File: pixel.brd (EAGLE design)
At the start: 160 x 100 mm, 13 parts, among them IC1 STM32F030K6TX-LQFP32(7X7), Y1 8 MHz

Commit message: blah
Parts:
- removed Y1: 8 MHz, crystals:CRYSTAL_SMD_3.2X2.5MM
- added C11: 0.1uF, rc:C0603
- added C12: 100 nF, rc:C0603
- added C13: 1nF, rc:C1206
- added CON1, CON2: DS1066-07M-SIDE, pixel_masterlib:DS1066-08M_SIDE
- added D1: SMF05C, pixel_masterlib:SC70_6L
- added D2: SMAJ12A, masterlib:SMA
- added IC2: ESDA6V1L, pixel_masterlib:SOT23
- added IC3: ST3485SOIC8, pixel_masterlib:SOIC8
- added IC4, IC5: MC74VHC1GT125, pixel_masterlib:SOT23-5
- added L1: 47UH, power_inductors:SDR0604
- added Q1: FDC6420C, pixel_masterlib:SOT23-6
- added R11, R12, R4, R5: 22R, rc:R0805
- added R2, R3: 560R, rc:R0603
- added R6: 10K, rc:R0805
- added R9: 60R, rc:R0603
- added RN1, RN2: 510R, pixel_masterlib:CAT16-J4
- added SJ1, SJ2: (no value), eth_conv_master_lib:RES_0
- added Z1: 16MHz, watchdog_master_library:OSCILLATOR-3.2X2.5
- C1: value 4.7 uF -> 100 nF
- R1: value (none) -> 60R
- moved C1 51.1 mm to (-18.0, -62.0)
- moved IC1 29.4 mm to (-6.00, -33.0)
- moved C2 28.3 mm to (-6.00, -46.0)
- moved C4 24.8 mm to (18.0, -46.0)
- moved C3 23.6 mm to (-2.00, -46.0)
- moved C5 18.2 mm to (12.0, -46.0)
- moved R1 15.9 mm to (-11.0, -50.0)
- moved C7 11.7 mm to (2.00, -46.0)
- moved C8 8.62 mm to (6.00, -46.0)
- moved C6 7.65 mm to (9.00, -46.0)
- moved C10 4.84 mm to (4.00, -50.0)
- moved C9 1.74 mm to (1.00, -50.0)
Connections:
- net LED1_FB renamed RE/DE
- new net A: D2.A, IC2.2, IC3.6, R1.2, R11.1, R11.2, R3.2
- new net B: D2.C, IC2.3, IC3.7, R12.1, R12.2, R2.1, SJ2.1
- new net CLOCK_BUFFERED: IC4.4, RN2.2
- new net DATA_IN: D1.4, RN1.1
- new net DATA_OUT: RN2.1
- new net DE: IC3.2, IC3.3
- new net LATCH_BUFFERED: IC5.4, RN2.3
- new net N$10: R9.1, SJ2.2
- new net N$11: C13.P$1, SJ1.2
- new net N$12: CON2.6, RN2.6
- new net N$13: Q1.1, R4.2
- new net N$14: R4.1
- new net N$15: Q1.6, R5.1
- new net N$16: Q1.2
- new net N$4: CON1.5, RN1.7
- new net N$5: CON1.6, RN1.6
- new net N$6: CON2.4, RN2.8
- new net N$7: Q1.3, R5.2, R6.2
- new net N$8: R1.1, R9.2, SJ1.1
- new net N$9: CON2.5, RN2.7
- new net RS485_A: CON1.2, CON2.2
- new net RS485_B: CON1.3, CON2.3
- new net VDD_12V: Q1.4, R6.1
- new net VDD_24V: CON1.1, CON2.1
- net CLOCK: now also D1.5, IC4.2, RN1.2
- net GND: now also C10.2, C11.1, C12.1, C13.P$2, CON1.7, CON2.7, D1.2, IC2.1, IC3.5, IC4.3, IC5.3, Q1.5, R3.1, Z1.2, Z1.4; no longer C10.1, Y1.2, Y1.4
- net LATCH: now also D1.6, IC5.2, RN1.3
- net N$1: now also Z1.1; no longer Y1.3
- net N$2: now also CON1.4, RN1.8; no longer IC1.3, R1.1
- net N$3: now also C10.1, IC1.3, Z1.3; no longer C10.2, R1.2, Y1.1
- net RX: now also IC3.1
- net TX: now also IC3.4
- net VDD_3V3: now also C11.2, C12.2, IC3.8, IC4.5, IC5.5, R2.2
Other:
- board outline removed

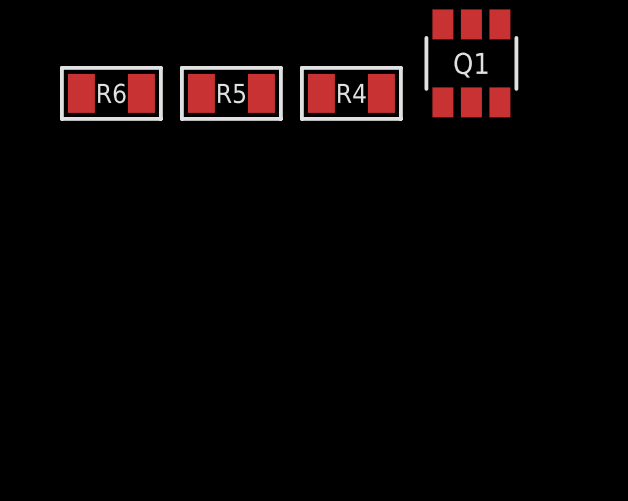
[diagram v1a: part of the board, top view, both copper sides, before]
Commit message: Preliminary LED driver
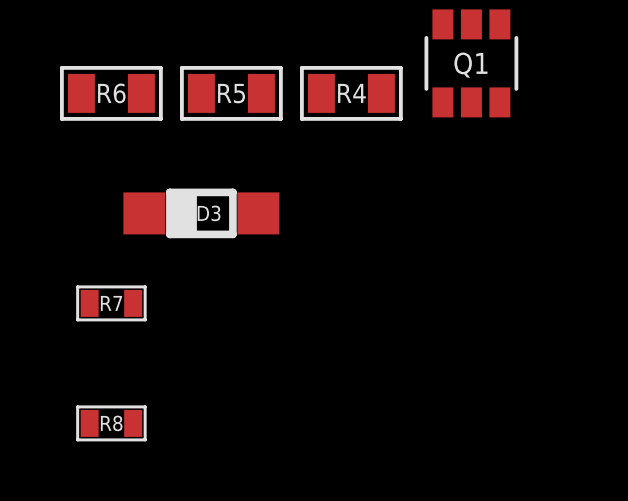
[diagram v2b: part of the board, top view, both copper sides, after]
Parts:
- added D3: (no value), diodes:SOD123
- added R7, R8: (no value), rc:R0603
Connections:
- removed net N$14: R4.1
- removed net N$16: Q1.2
- new net LED1_A: L1.2
- new net LED1_FB\: R7.1
- new net LED_COMMON_C: R7.2, R8.2
- new net N$17: D3.C, L1.1, Q1.2
- net GND: now also D3.A, R8.1
- net LED1_PWM: now also R4.1
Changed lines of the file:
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@@
 <attribute name="PACKAGE" value="0805" x="-46" y="-65" size="1.778" layer="27" display="off"/>
+</element>
+<element name="D3" library="diodes" package="SOD123" value="" x="-43" y="-69">
+<attribute name="PACKAGE" value="SOD123" x="-43" y="-69" size="1.778" layer="27" display="off"/>
+</element>
+<element name="R7" library="rc" package="R0603" value="" x="-46" y="-72">
+<attribute name="PACKAGE" value="0603" x="-46" y="-72" size="1.778" layer="27" display="off"/>
+</element>
+<element name="R8" library="rc" package="R0603" value="" x="-46" y="-76">
+<attribute name="PACKAGE" value="0603" x="-46" y="-76" size="1.778" layer="27" display="off"/>
 </element>
 </elements>
@@
 <contactref element="C12" pad="1"/>
 <contactref element="Q1" pad="5"/>
+<contactref element="D3" pad="A"/>
+<contactref element="R8" pad="1"/>
+<wire x1="-41.1" y1="-69" x2="-46.725" y2="-76" width="0" layer="19" extent="1-1"/>
+<wire x1="-34" y1="-62.7" x2="-41.1" y2="-69" width="0" layer="19" extent="1-1"/>
 <wire x1="-18.725" y1="-62" x2="-34" y2="-62.7" width="0" layer="19" extent="1-1"/>
 <wire x1="-18.725" y1="-66" x2="-18.725" y2="-62" width="0" layer="19" extent="1-1"/>
@@
 <signal name="LED1_PWM">
 <contactref element="IC1" pad="18"/>
+<contactref element="R4" pad="1"/>
+<wire x1="-1.75" y1="-35" x2="-39" y2="-65" width="0" layer="19" extent="1-1"/>
 </signal>
 <signal name="LED2_PWM">
@@
 <wire x1="-34.95" y1="-65.3" x2="-37" y2="-65" width="0" layer="19" extent="1-1"/>
 </signal>
-<signal name="N$14">
-<contactref element="R4" pad="1"/>
-</signal>
 <signal name="VDD_12V">
 <contactref element="Q1" pad="4"/>
 <contactref element="R6" pad="1"/>
 <wire x1="-33.05" y1="-62.7" x2="-47" y2="-65" width="0" layer="19" extent="1-1"/>
-</signal>
-<signal name="N$16">
-<contactref element="Q1" pad="2"/>
 </signal>
 <signal name="N$7">
@@
 <wire x1="-34.95" y1="-62.7" x2="-43" y2="-65" width="0" layer="19" extent="1-1"/>
 </signal>
+<signal name="N$17">
+<contactref element="D3" pad="C"/>
+<contactref element="Q1" pad="2"/>
+<contactref element="L1" pad="1"/>
+<wire x1="-34" y1="-65.3" x2="-44.9" y2="-69" width="0" layer="19" extent="1-1"/>
+<wire x1="-29.95" y1="-57" x2="-34" y2="-65.3" width="0" layer="19" extent="1-1"/>
+</signal>
+<signal name="LED1_FB\">
+<contactref element="R7" pad="1"/>
+</signal>
+<signal name="LED1_A">
+<contactref element="L1" pad="2"/>
+</signal>
+<signal name="LED_COMMON_C">
+<contactref element="R8" pad="2"/>
+<contactref element="R7" pad="2"/>
+<wire x1="-45.275" y1="-72" x2="-45.275" y2="-76" width="0" layer="19" extent="1-1"/>
+</signal>
 </signals>

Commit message: minor changes
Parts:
- removed D3: (no value), diodes:SOD123
- removed R8: (no value), rc:R0603
- added C14: 10uF 6.3V, rc:C1206
- added D4: CRS08-SOD123, eth_conv_master_lib:SOD123
- added NRF24L01: NRF24L01, ali_modules:NRF24L01
- R7: value (none) -> 2R; device rc:R0603 -> rc:R1206
- moved R7 4.47 mm to (-50.0, -74.0)
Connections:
- removed net LED1_A: L1.2
- removed net LED1_FB\: R7.1
- removed net LED_COMMON_C: R7.2, R8.2
- new net MISO: IC1.27, NRF24L01.7
- new net MOSI: IC1.28, NRF24L01.6
- new net NRF_CE: NRF24L01.3
- new net NRF_CSN: NRF24L01.4
- new net NRF_IRQ: NRF24L01.8
- new net SCK: IC1.26, NRF24L01.5
- net GND: now also C14.P$2, D4.A, NRF24L01.1, R7.P$1; no longer D3.A, R8.1
- net N$17: now also D4.C; no longer D3.C
- net VDD_3V3: now also C14.P$1, NRF24L01.2
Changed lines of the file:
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@@
 <attribute name="PACKAGE" value="0805" x="-46" y="-65" size="1.778" layer="27" display="off"/>
 </element>
-<element name="D3" library="diodes" package="SOD123" value="" x="-43" y="-69">
-<attribute name="PACKAGE" value="SOD123" x="-43" y="-69" size="1.778" layer="27" display="off"/>
+<element name="R7" library="rc" package="R1206" value="2R" x="-50" y="-74">
+<attribute name="PACKAGE" value="1206" x="-50" y="-74" size="1.778" layer="27" display="off"/>
 </element>
-<element name="R7" library="rc" package="R0603" value="" x="-46" y="-72">
-<attribute name="PACKAGE" value="0603" x="-46" y="-72" size="1.778" layer="27" display="off"/>
+<element name="D4" library="eth_conv_master_lib" package="SOD123" value="CRS08-SOD123" x="-47" y="-78">
+<attribute name="MANF#" value="CRS08(TE85L,Q,M)" x="-47" y="-78" size="1.778" layer="27" display="off"/>
+<attribute name="MANF" value="Toshiba Semiconductor and Storage" x="-47" y="-78" size="1.778" layer="27" display="off"/>
+<attribute name="DIGIKEY#" value="CRS08QMCT-ND" x="-47" y="-78" size="1.778" layer="27" display="off"/>
 </element>
-<element name="R8" library="rc" package="R0603" value="" x="-46" y="-76">
-<attribute name="PACKAGE" value="0603" x="-46" y="-76" size="1.778" layer="27" display="off"/>
+<element name="NRF24L01" library="ali_modules" package="NRF24L01" value="NRF24L01" x="-30" y="-95"/>
+<element name="C14" library="rc" package="C1206" value="10uF 6.3V" x="-50" y="-108">
+<attribute name="PACKAGE" value="1206" x="-55" y="-102" size="1.778" layer="27" display="off"/>
 </element>
 </elements>
@@
 <contactref element="IC5" pad="5"/>
 <contactref element="C12" pad="2"/>
+<contactref element="NRF24L01" pad="2"/>
+<contactref element="C14" pad="P$1"/>
+<wire x1="-40.16" y1="-88.65" x2="-51.55" y2="-108" width="0" layer="19" extent="1-1"/>
+<wire x1="-17.275" y1="-66" x2="-40.16" y2="-88.65" width="0" layer="19" extent="1-1"/>
 <wire x1="-17.275" y1="-62" x2="-17.275" y2="-66" width="0" layer="19" extent="1-1"/>
 <wire x1="-15.95" y1="-54.7" x2="-17.275" y2="-62" width="0" layer="19" extent="1-1"/>
@@
 </signal>
 <signal name="GND">
-<contactref element="C2" pad="1"/>
 <contactref element="C3" pad="1"/>
 <contactref element="C4" pad="1"/>
@@
 <contactref element="C12" pad="1"/>
 <contactref element="Q1" pad="5"/>
-<contactref element="D3" pad="A"/>
-<contactref element="R8" pad="1"/>
-<wire x1="-41.1" y1="-69" x2="-46.725" y2="-76" width="0" layer="19" extent="1-1"/>
-<wire x1="-34" y1="-62.7" x2="-41.1" y2="-69" width="0" layer="19" extent="1-1"/>
+<contactref element="R7" pad="P$1"/>
+<contactref element="D4" pad="A"/>
+<contactref element="NRF24L01" pad="1"/>
+<contactref element="C14" pad="P$2"/>
+<contactref element="C2" pad="1"/>
+<wire x1="-42.7" y1="-88.65" x2="-48.45" y2="-108" width="0" layer="19" extent="1-1"/>
+<wire x1="-45.3" y1="-78" x2="-42.7" y2="-88.65" width="0" layer="19" extent="1-1"/>
+<wire x1="-51.55" y1="-74" x2="-45.3" y2="-78" width="0" layer="19" extent="1-1"/>
+<wire x1="-34" y1="-62.7" x2="-45.3" y2="-78" width="0" layer="19" extent="1-1"/>
 <wire x1="-18.725" y1="-62" x2="-34" y2="-62.7" width="0" layer="19" extent="1-1"/>
 <wire x1="-18.725" y1="-66" x2="-18.725" y2="-62" width="0" layer="19" extent="1-1"/>
@@
 </signal>
 <signal name="N$17">
-<contactref element="D3" pad="C"/>
 <contactref element="Q1" pad="2"/>
 <contactref element="L1" pad="1"/>
-<wire x1="-34" y1="-65.3" x2="-44.9" y2="-69" width="0" layer="19" extent="1-1"/>
+<contactref element="D4" pad="C"/>
+<wire x1="-34" y1="-65.3" x2="-48.7" y2="-78" width="0" layer="19" extent="1-1"/>
 <wire x1="-29.95" y1="-57" x2="-34" y2="-65.3" width="0" layer="19" extent="1-1"/>
 </signal>
-<signal name="LED1_FB\">
-<contactref element="R7" pad="1"/>
-</signal>
-<signal name="LED1_A">
-<contactref element="L1" pad="2"/>
-</signal>
-<signal name="LED_COMMON_C">
-<contactref element="R8" pad="2"/>
-<contactref element="R7" pad="2"/>
-<wire x1="-45.275" y1="-72" x2="-45.275" y2="-76" width="0" layer="19" extent="1-1"/>
+<signal name="NRF_CSN">
+<contactref element="NRF24L01" pad="4"/>
+</signal>
+<signal name="NRF_CE">
+<contactref element="NRF24L01" pad="3"/>
+</signal>
+<signal name="SCK">
+<contactref element="IC1" pad="26"/>
+<contactref element="NRF24L01" pad="5"/>
+<wire x1="-4" y1="-28.75" x2="-42.7" y2="-93.73" width="0" layer="19" extent="1-1"/>
+</signal>
+<signal name="MISO">
+<contactref element="IC1" pad="27"/>
+<contactref element="NRF24L01" pad="7"/>
+<wire x1="-4.8" y1="-28.75" x2="-42.7" y2="-96.27" width="0" layer="19" extent="1-1"/>
+</signal>
+<signal name="MOSI">
+<contactref element="IC1" pad="28"/>
+<contactref element="NRF24L01" pad="6"/>
+<wire x1="-5.6" y1="-28.75" x2="-40.16" y2="-93.73" width="0" layer="19" extent="1-1"/>
+</signal>
+<signal name="NRF_IRQ">
+<contactref element="NRF24L01" pad="8"/>
 </signal>
 </signals>
